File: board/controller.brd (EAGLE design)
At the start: 100 x 100 mm, 69 parts, among them J1 COOLANT, J10 FEED_HOLD, J11 SD_READER, J12 RESET, J13 Z, J14 GND, J15 Z_DISPLAY, J18 DISPLAY, J19 A, J2 PROBE, J20 HOLDING, J22 WHEEL, J23 SPINDLE, J24 +5V, J26 GND, J3 MOTOR_CURRENT, J4 X, J6 ERROR, J8 CYCLE_START, J9 Y, U100 SENSOR-IR-THRU

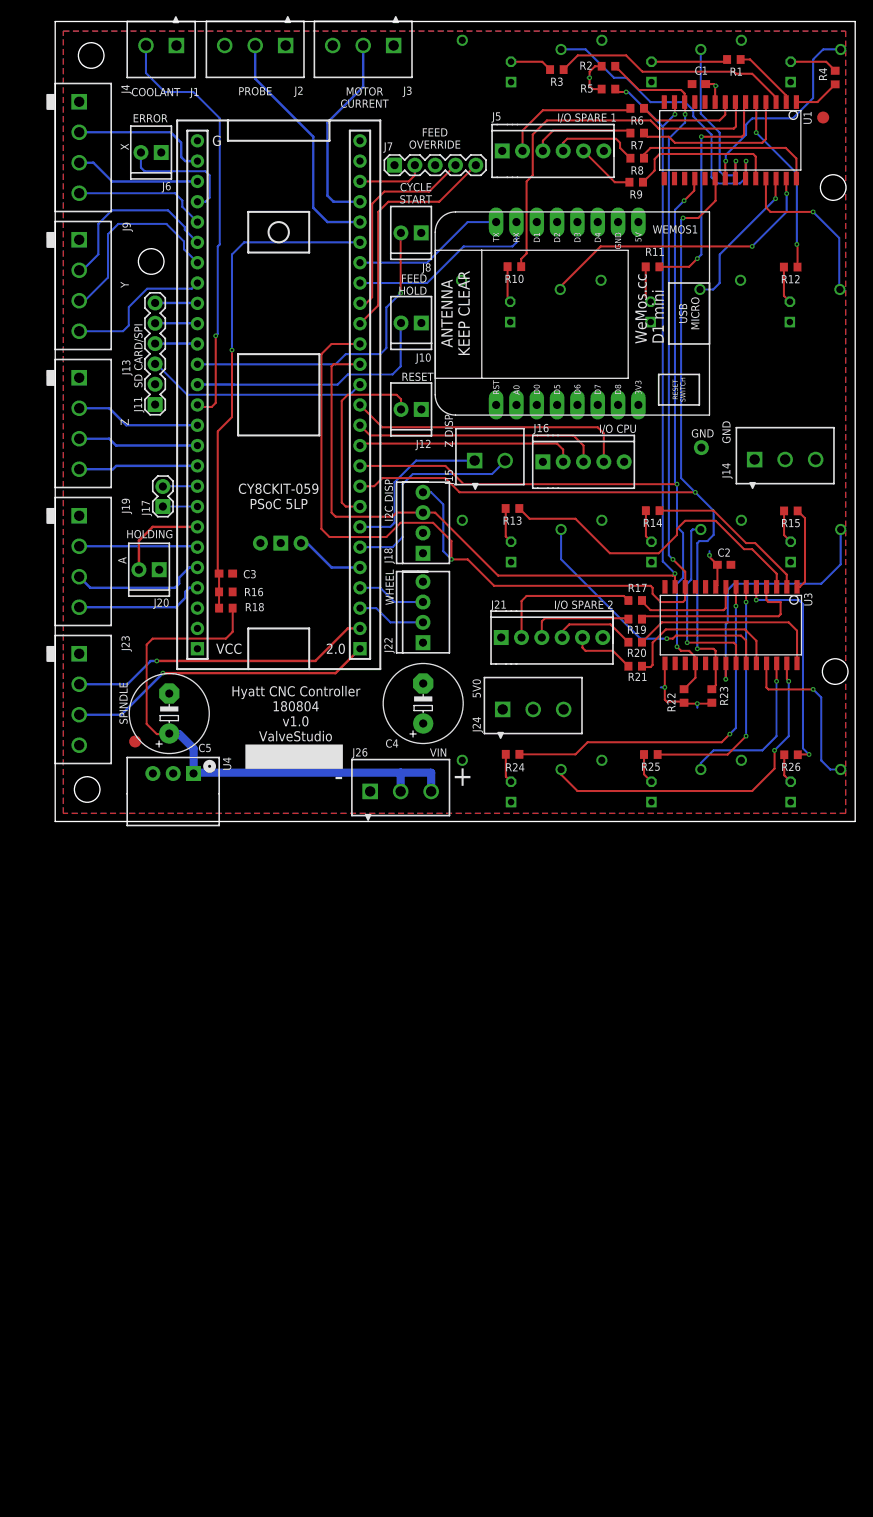
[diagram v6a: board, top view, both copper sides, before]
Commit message: re-organizing pin layout due to creator optimization
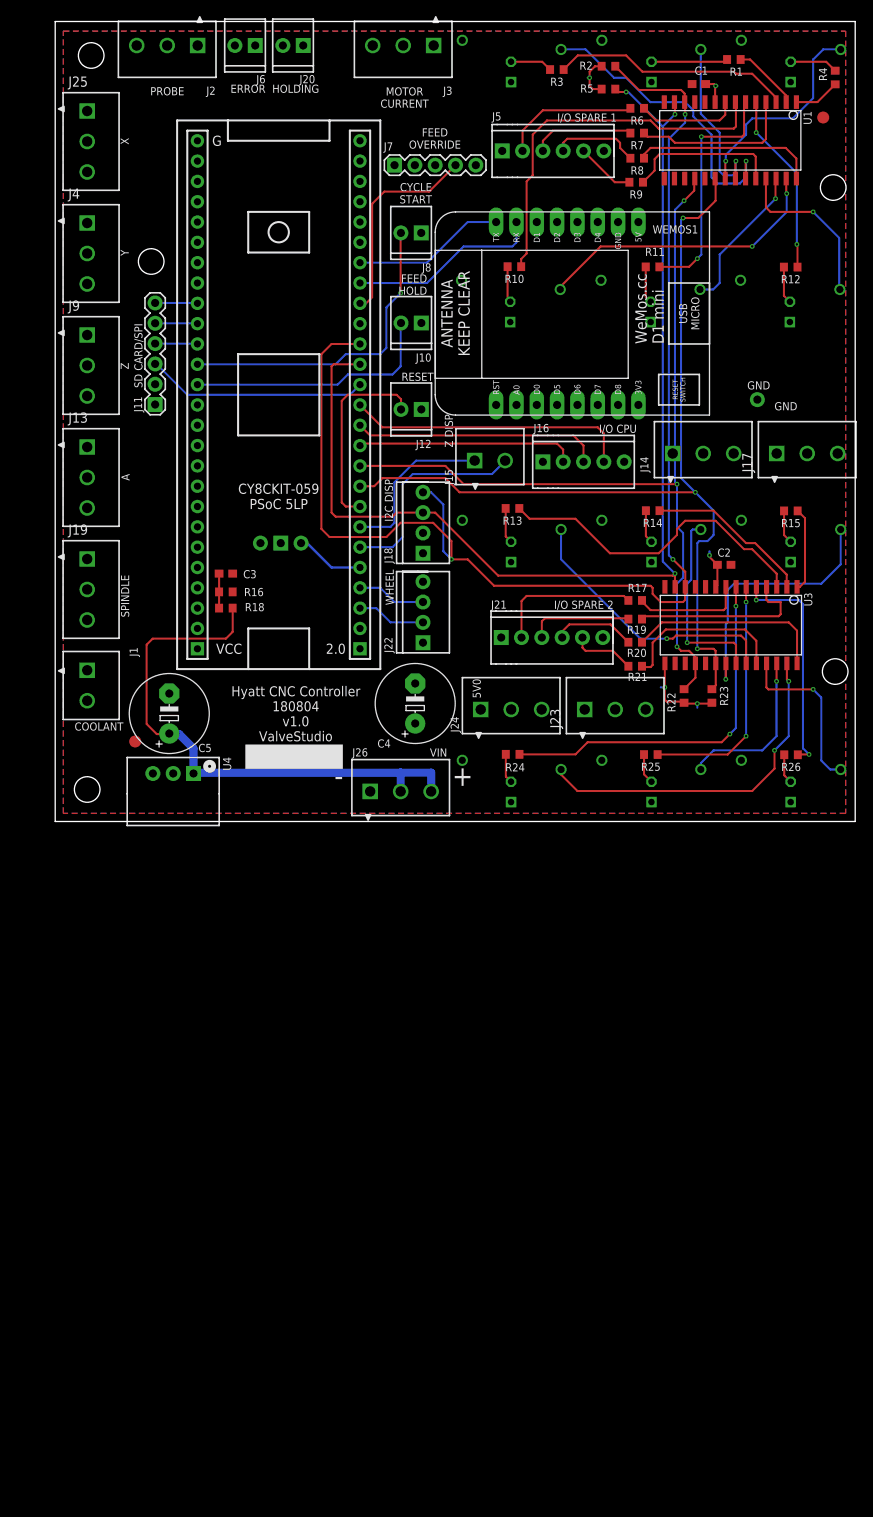
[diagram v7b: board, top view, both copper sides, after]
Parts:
- added J25: X, holla:CONN-3.81MM-KF2EDG-3
- J13: value Z -> A; device holla:CONN-3.81MM-KF2EDG-4 -> holla:CONN-3.81MM-KF2EDG-3
- J17: value (none) -> +5V; device holla:1X02 -> holla:CONN-3.81MM-KF2EDG-3
- J19: value A -> SPINDLE; device holla:CONN-3.81MM-KF2EDG-4 -> holla:CONN-3.81MM-KF2EDG-3
- J23: value SPINDLE -> GND; device holla:CONN-3.81MM-KF2EDG-4 -> holla:CONN-3.81MM-KF2EDG-3
- J4: value X -> Y; device holla:CONN-3.81MM-KF2EDG-4 -> holla:CONN-3.81MM-KF2EDG-3
- J9: value Y -> Z; device holla:CONN-3.81MM-KF2EDG-4 -> holla:CONN-3.81MM-KF2EDG-3
- moved J17 80.8 mm to (94.0, 46.0), turned to 0 degrees
- moved J1 80.5 mm to (4.00, 17.0), turned to 270 degrees
- moved J20 68.0 mm to (31.0, 97.0)
- moved J23 67.0 mm to (70.0, 14.0), turned to 0 degrees
- moved J6 17.8 mm to (25.0, 97.0)
- moved J4 13.3 mm to (4.00, 71.0)
- moved J2 11.0 mm to (14.0, 97.0)
- moved J14 10.3 mm to (81.0, 46.0)
- moved J9 10.0 mm to (4.00, 57.0)
- moved GND 9.22 mm to (87.8, 52.7)
- moved J13 6.82 mm to (4.00, 43.0)
- moved J3 5.00 mm to (43.5, 97.0)
- moved J19 3.64 mm to (4.00, 29.0)
- moved J24 2.75 mm to (57.0, 14.0)
- moved C4 1.00 mm to (45.0, 14.8)
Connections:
- removed net N$43: J17.2, U2.0.2
- removed net N$45: J17.1, U2.0.3
- new net SPINDLE_SPEED: J19.3
- new net VIN_SCALED_IN: U2.2.0
- net 5V0: now also J17.1, J17.2, J17.3; no longer J23.4
- net A_DIRECTION_OUT: now also J13.1; no longer J19.4
- net A_LIMIT_IN: now also J13.3; no longer J19.2
- net A_STEP_OUT: now also J13.2; no longer J19.3
- net COOLANT_ENABLE_OUT: no longer U2.15.4
- net FEED_OVERRIDE_BTN: no longer U2.1.0
- net FEED_OVERRIDE_IN: now also U2.1.4; no longer U2.1.7
- net GND: now also J23.2, J23.3; no longer J13.1, J19.1, J4.1, J9.1
- net MOTOR_CURRENT_IN: now also U2.1.0
- net PROBE_IN: now also U2.3.0; no longer U2.1.5
- net SPINDLE_DIRECTION_OUT: now also J19.2; no longer J23.3, U2.2.0
- net SPINDLE_ENABLE_OUT: now also J19.1; no longer J23.2
- net VIN_SCALE: no longer U2.1.4
- net X_DIRECTION_OUT: now also J25.1; no longer J4.4
- net X_LIMIT_IN: now also J25.3; no longer J4.2, U2.3.0
- net X_STEP_OUT: now also J25.2; no longer J4.3
- net Y_DIRECTION_OUT: now also J4.1; no longer J9.4
- net Y_LIMIT_IN: now also J4.3; no longer J9.2
- net Y_STEP_OUT: now also J4.2; no longer J9.3
- net Z_DIRECTION_OUT: now also J9.1; no longer J13.4
- net Z_LIMIT_IN: now also J9.3; no longer J13.2
- net Z_STEP_OUT: now also J9.2; no longer J13.3
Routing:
- net VIN_SCALE: track 61.9 -> 4.55 mm, vias 1 -> 0
- net COOLANT_ENABLE_OUT: track 53.4 -> 0.00 mm, vias 1 -> 0
- net SPINDLE_DIRECTION_OUT: track 38.5 -> 0.00 mm, vias 1 -> 0
- net SPINDLE_ENABLE_OUT: track 38.0 -> 0.00 mm, vias 1 -> 0
- net PROBE_IN: track 29.9 -> 0.00 mm
- net FEED_OVERRIDE_BTN: track 29.5 -> 0.00 mm
- net MOTOR_CURRENT_IN: track 25.0 -> 0.00 mm
- net Y_STEP_OUT: track 24.5 -> 0.00 mm
- net Y_LIMIT_IN: track 22.0 -> 0.00 mm
- net Y_DIRECTION_OUT: track 18.6 -> 0.00 mm
- net X_LIMIT_IN: track 17.3 -> 0.00 mm
- net A_STEP_OUT: track 16.9 -> 0.00 mm
- net X_DIRECTION_OUT: track 16.7 -> 0.00 mm
- net A_DIRECTION_OUT: track 16.2 -> 0.00 mm
- net X_STEP_OUT: track 15.7 -> 0.00 mm
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
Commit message: reworked connector positions and pin mapping
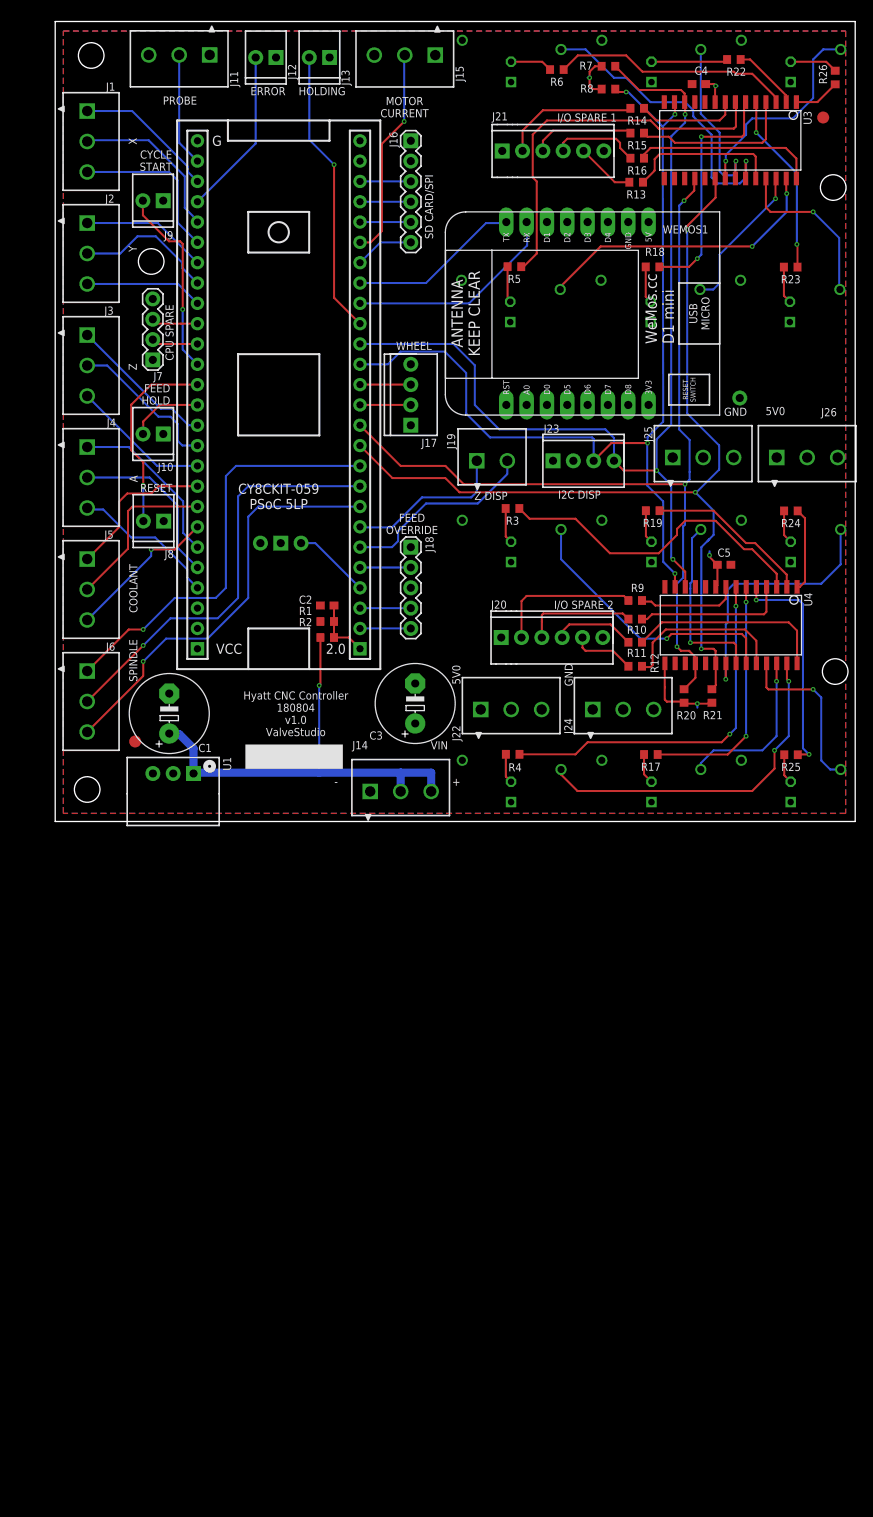
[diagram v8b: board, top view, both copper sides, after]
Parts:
- C1: value (none) -> 47u; device holla:C0603 -> holla:E5-10
- C2: value (none) -> 1u
- C3: value 1u -> 47u; device holla:C0603 -> holla:E5-10
- C4, C5: value 47u -> (none); device holla:E5-10 -> holla:C0603
- J1: value COOLANT -> X; device holla:CONN-3.81MM-KF2EDG-2 -> holla:CONN-3.81MM-KF2EDG-3
- J11: value SD_READER -> PROBE; device holla:1X06 -> holla:CONN-3.81MM-KF2EDG-3
- J12: value RESET -> ERROR
- J13: value A -> HOLDING; device holla:CONN-3.81MM-KF2EDG-3 -> holla:CONN-.100-2
- J15: value Z_DISPLAY -> MOTOR_CURRENT; device holla:CONN-3.81MM-KF2EDG-2 -> holla:CONN-3.81MM-KF2EDG-3
- J16: value (none) -> SD_READER; device holla:CONN-.100-5 -> holla:1X06
- J17: value +5V -> WHEEL; device holla:CONN-3.81MM-KF2EDG-3 -> holla:CONN-.100-4
- J18: value DISPLAY -> (none); device holla:CONN-.100-4 -> holla:1X05
- J19: value SPINDLE -> Z_DISPLAY; device holla:CONN-3.81MM-KF2EDG-3 -> holla:CONN-3.81MM-KF2EDG-2
- J2: value PROBE -> Y
- J20: value HOLDING -> (none); device holla:CONN-.100-2 -> holla:CONN-.100-6
- J22: value WHEEL -> +5V; device holla:CONN-.100-4 -> holla:CONN-3.81MM-KF2EDG-3
- J23: value GND -> DISPLAY; device holla:CONN-3.81MM-KF2EDG-3 -> holla:CONN-.100-4
- J24: value +5V -> GND
- J25: value X -> GND
- J26: value GND -> +5V
- J3: value MOTOR_CURRENT -> Z
- J4: value Y -> A
- J5: value (none) -> COOLANT; device holla:CONN-.100-6 -> holla:CONN-3.81MM-KF2EDG-3
- J6: value ERROR -> SPINDLE; device holla:CONN-.100-2 -> holla:CONN-3.81MM-KF2EDG-3
- J7: device holla:1X05 -> holla:1X04
- J8: value CYCLE_START -> RESET
- J9: value Z -> CYCLE_START; device holla:CONN-3.81MM-KF2EDG-3 -> holla:CONN-.100-2
- R2, R5: value 2.2k -> (none)
- R20, R21: value (none) -> 10k
- R22, R23: value 10k -> (none)
- R7, R8: value (none) -> 2.2k
- U1: device holla:SO28W -> holla:VREG-SIP3
- U4: device holla:VREG-SIP3 -> holla:SO28W
- moved U1 105.8 mm to (14.8, 6.00)
- moved C1 102.8 mm to (14.3, 13.5), turned to 90 degrees
- moved R4 93.7 mm to (57.2, 8.39), turned to 180 degrees
- moved R1 86.7 mm to (34.0, 25.0), turned to 0 degrees
- moved J25 86.5 mm to (81.0, 45.5), turned to 0 degrees
- moved C4 85.2 mm to (80.5, 92.2), turned to 180 degrees
- moved R26 84.8 mm to (97.5, 93.0), turned to 90 degrees
- moved J6 84.6 mm to (4.00, 15.0), turned to 270 degrees
- moved R22 79.8 mm to (84.8, 95.2), turned to 180 degrees
- moved R2 79.6 mm to (34.0, 23.0)
- moved J20 78.0 mm to (55.8, 23.0), turned to 0 degrees
- moved J5 75.5 mm to (4.00, 29.0), turned to 270 degrees
- moved R16 74.7 mm to (72.8, 82.9)
- moved U4 72.8 mm to (85.1, 24.5)
- moved C5 71.8 mm to (83.6, 32.1), turned to 0 degrees
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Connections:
- removed net COOLANT_ENABLE_OUT: J1.2
- removed net P12.3: J16.4, U2.12.3
- removed net P12.4: J16.3, U2.12.4
- removed net P12.5: J16.2, U2.12.5
- removed net SD_READER_CS: J11.4, U2.15.1
- removed net VIN_SCALE: C3.1, R16.2, R18.1
- new net COOLANT_SPARE: J5.3, U2.0.4
- new net CPU_SPARE_IO_0: J7.3, U2.15.0
- new net CPU_SPARE_IO_1: J7.2, U2.15.1
- new net FLOOD_ENABLE_OUT: J5.1, U2.0.2
- new net MIST_ENABLE_OUT: J5.2, U2.0.3
- new net SD_CARD_CS: J16.4, U2.1.6
- net !IO_INT: now also R21.1, U2.12.5, U4.20; no longer R23.1, U1.20, U2.12.7
- net !IO_RESET: now also R20.1, U2.12.4, U4.18; no longer R22.1, U1.18, U2.12.6
- net 5V0: now also C3.+, C4.1, C5.1, J11.3, J15.3, J16.1, J17.4, J18.3, J20.6, J22.1, J22.2, J22.3, J23.2, J26.1, J26.2, J26.3, J7.4, R20.2, R21.2, R7.2, R8.2, U1.3, U4.15, U4.9; no longer C1.1, C2.1, C4.+, J11.1, J16.5, J17.1, J17.2, J17.3, J18.2, J2.3, J22.4, J24.1, J24.2, J24.3, J3.3, J5.6, J7.3, R2.2, R22.2, R23.2, R5.2, U1.9, U3.15, U4.3
- net A_DIRECTION_OUT: now also J4.1, U2.0.5; no longer J13.1, U2.0.7
- net A_LIMIT_IN: now also J4.3, U2.0.7; no longer J13.3, U2.0.5
- net A_STEP_OUT: now also J4.2; no longer J13.2
- net CYCLE_START_IN: now also J9.2; no longer J8.2
- net ERROR_INDICATOR_OUT: now also J12.2; no longer J6.2
- net FEED_HOLDING_OUT: now also J13.2, U2.1.0; no longer J20.2, U2.0.4
- net FEED_HOLD_IN: now also U2.15.4; no longer U2.15.3
- net FEED_OVERRIDE_BTN: now also J18.5, U2.2.1; no longer J7.5
- net FEED_OVERRIDE_IN: now also J18.2, U2.2.4; no longer J7.2, U2.1.4
- net FEED_OVERRIDE_OFF: now also J18.4, U2.2.2; no longer J7.4, U2.1.1
- net GND: now also C1.-, C3.-, C4.2, C5.2, J11.1, J13.1, J15.1, J16.2, J17.1, J24.1, J24.2, J24.3, J25.1, J25.2, J25.3, J9.1, R1.1, U1.2, U3.15, U4.10, U4.16, U4.17; no longer C1.2, C3.2, C4.-, C5.-, J1.1, J11.2, J14.2, J14.3, J16.1, J2.1, J22.1, J23.2, J23.3, J26.1, J3.1, J5.1, J6.1, R16.1, U1.10, U1.15, U1.16, U1.17, U4.2
- net I2C_SCL: now also J23.4, R7.1, U4.12; no longer J18.4, R2.1, U1.12
- net I2C_SDA: now also J23.3, R8.1, U4.13; no longer J18.3, R5.1, U1.13
- net IR_RECEIVE_IN: now also U2.2.3; no longer U2.2.4
- net MOTOR_CURRENT_IN: now also J15.2, U2.1.4; no longer J3.2, U2.1.0, U2.1.6
- net N$1: now also R26.1, U3.1; no longer R4.1, U1.1
- net N$10: now also J20.5, R12.2; no longer J21.5, R21.2
- net N$11: now also J20.4, R11.2; no longer J21.4, R20.2
- net N$15: now also R6.1, U3.3; no longer R3.1, U1.3
- net N$16: now also R15.1, U3.4; no longer R7.1, U1.4
- net N$17: now also R23.1, U3.5; no longer R12.1, U1.5
- net N$18: now also R18.1, U3.6; no longer R11.1, U1.6
- net N$19: now also R5.1, U3.7; no longer R10.1, U1.7
- net N$2: now also R22.1, U3.2; no longer R1.1, U1.2
- net N$20: now also R14.1, U3.8; no longer R6.1, U1.8
- net N$21: now also R24.1, U4.1; no longer R15.1, U3.1
- net N$22: now also R19.1, U4.2; no longer R14.1, U3.2
- net N$23: now also R3.1, U4.3; no longer R13.1, U3.3
- net N$24: now also R10.1, U4.4; no longer R19.1, U3.4
- net N$25: now also R25.1, U4.5; no longer R26.1, U3.5
- net N$26: now also R17.1, U4.6; no longer R25.1, U3.6
- net N$27: now also R4.1, U4.7; no longer R24.1, U3.7
- net N$28: now also R9.1, U4.8; no longer R17.1, U3.8
- net N$3: now also R13.1, U3.24; no longer R9.1, U1.24
- net N$30: now also J21.2, R14.2; no longer J5.2, R6.2
- net N$4: now also J21.5, R13.2; no longer J5.5, R9.2
- net N$44: now also J20.3, R10.2; no longer J21.3, R19.2
- net N$48: now also J20.2, R9.2; no longer J21.2, R17.2
- net N$5: now also R16.1, U3.28; no longer R8.1, U1.28
- net N$6: now also J21.3, R15.2; no longer J5.3, R7.2
- net N$7: now also J21.4, R16.2; no longer J5.4, R8.2
- net N$8: now also R12.1, U4.24; no longer R21.1, U3.24
- net N$9: now also R11.1, U4.28; no longer R20.1, U3.28
- net PROBE_IN: now also J11.2; no longer J2.2
- net RADIO_RX: now also U2.1.1; no longer U2.1.2
- net RADIO_TX: now also U2.1.2; no longer U2.1.3
- net RESET_IN: now also J8.2, U2.15.3; no longer J12.2, U2.2.7
- net S1A1: now also U3.21; no longer U1.21
- net S1AA: now also R26.2; no longer R4.2
- net S1B1: now also U3.22; no longer U1.22
- net S1BA: now also R22.2; no longer R1.2
- net S1C1: now also U3.23; no longer U1.23
- net S1CA: now also R6.2; no longer R3.2
- net S2A1: now also S100.A_1, U3.25; no longer S102.A_1, U1.25
- net S2AA: now also R23.2, S100.A_A; no longer R12.2, S102.A_A
- net S2B1: now also S100.B_1, U3.26; no longer S102.B_1, U1.26
- net S2BA: now also R18.2, S100.B_A; no longer R11.2, S102.B_A
- net S2C1: now also S100.C_1, U3.27; no longer S102.C_1, U1.27
- net S2CA: now also R5.2, S100.C_A; no longer R10.2, S102.C_A
- net S3A1: now also S102.A_1, U4.21; no longer S101.A_1, U3.21
- net S3AA: now also R24.2, S102.A_A; no longer R15.2, S101.A_A
- net S3B1: now also S102.B_1, U4.22; no longer S101.B_1, U3.22
- net S3BA: now also R19.2, S102.B_A; no longer R14.2, S101.B_A
- net S3C1: now also S102.C_1, U4.23; no longer S101.C_1, U3.23
- net S3CA: now also R3.2, S102.C_A; no longer R13.2, S101.C_A
- net S4A1: now also S101.A_1, U4.25; no longer S100.A_1, U3.25
- net S4AA: now also R25.2, S101.A_A; no longer R26.2, S100.A_A
- net S4B1: now also S101.B_1, U4.26; no longer S100.B_1, U3.26
- net S4BA: now also R17.2, S101.B_A; no longer R25.2, S100.B_A
- net S4C1: now also S101.C_1, U4.27; no longer S100.C_1, U3.27
- net S4CA: now also R4.2, S101.C_A; no longer R24.2, S100.C_A
- net SPINDLE_DIRECTION_OUT: now also J6.2, U2.12.7; no longer J19.2
- net SPINDLE_ENABLE_OUT: now also J6.1, U2.12.6; no longer J19.1, U2.2.1
- net SPINDLE_SPEED: now also J6.3, U2.2.7; no longer J19.3
- net SPI_MISO: now also J16.6, U2.1.3; no longer J11.6, U2.3.7
- net SPI_MOSI: now also J16.3, U2.1.7; no longer J11.3, U2.12.2
- net SPI_SCK: now also J16.5, U2.1.5; no longer J11.5, U2.15.0
- net VIN: now also C1.+, J14.2, J14.3, R2.2, U1.1; no longer C5.+, J26.2, J26.3, R18.2, U4.1
- net VIN_SCALED_IN: now also C2.1, R1.2, R2.1
- net WHEEL_ENCODER_A_IN: now also J17.3, U2.12.2; no longer J22.3, U2.2.3
- net WHEEL_ENCODER_B_IN: now also J17.2, U2.12.3; no longer J22.2, U2.2.2
- net X_DIRECTION_OUT: now also J1.1, U2.3.1; no longer J25.1, U2.3.3
- net X_LIMIT_IN: now also J1.3, U2.3.4; no longer J25.3
- net X_STEP_OUT: now also J1.2, U2.3.3; no longer J25.2, U2.3.1
- net Y_DIRECTION_OUT: now also J2.1, U2.3.5; no longer J4.1, U2.3.6
- net Y_LIMIT_IN: now also J2.3, U2.3.7; no longer J4.3, U2.3.4
- net Y_STEP_OUT: now also J2.2, U2.3.6; no longer J4.2, U2.3.5
- net Z_DIRECTION_OUT: now also J3.1, U2.15.5; no longer J9.1, U2.0.1
- net Z_DISPLAY_RX_IN: now also J19.2; no longer J15.2
- net Z_DISPLAY_TX_OUT: now also J19.1; no longer J15.1
- net Z_LIMIT_IN: now also J3.3, U2.0.1; no longer J9.3, U2.15.5
- net Z_STEP_OUT: now also J3.2; no longer J9.2
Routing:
- net SPINDLE_ENABLE_OUT: track 0.00 -> 52.9 mm, vias 0 -> 1
- net SPINDLE_SPEED: track 0.00 -> 52.8 mm, vias 0 -> 1
- net SPINDLE_DIRECTION_OUT: track 0.00 -> 52.7 mm, vias 0 -> 1
- net I2C_SCL: track 165.4 -> 122.9 mm
- net FEED_HOLDING_OUT: track 0.00 -> 35.9 mm, vias 0 -> 1
- net P12.3: track 35.5 -> 0.00 mm
- net P12.4: track 31.0 -> 0.00 mm
- net P12.5: track 27.3 -> 0.00 mm
- net MOTOR_CURRENT_IN: track 0.00 -> 26.5 mm, vias 0 -> 1
- net FEED_HOLD_IN: track 31.8 -> 9.21 mm
- net A_STEP_OUT: track 0.00 -> 21.5 mm
- net SPI_MOSI: track 27.7 -> 6.35 mm
- net A_DIRECTION_OUT: track 0.00 -> 21.3 mm
- net ERROR_INDICATOR_OUT: track 0.00 -> 21.0 mm
- net MIST_ENABLE_OUT: track 0.00 -> 20.8 mm
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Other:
- board text added: "CPU SPARE"
- board text removed: "I/O CPU"
